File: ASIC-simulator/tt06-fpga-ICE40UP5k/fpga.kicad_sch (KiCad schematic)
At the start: 37 parts, among them U1 ICE40UP5K-SG48I, U2 AP2112K-1.2, X1 24MHz

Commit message: LCSC components and minor layout tweaks for production run
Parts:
- C1, C10, C12, C14, C15, C17, C3, C6, C8: LCSC (none) -> C60474
- C11, C7: LCSC (none) -> C29936
- C13, C16, C18, C2, C4, C9: LCSC (none) -> C237615
- C5: LCSC (none) -> C92487
- R10, R3: LCSC (none) -> C60490
- R11: LCSC (none) -> C106231
- R2, R6, R9: LCSC (none) -> C106232
- R5: LCSC (none) -> C106235
- R7, R8: LCSC (none) -> C163455
- TP1, TP2: now left out of the parts list

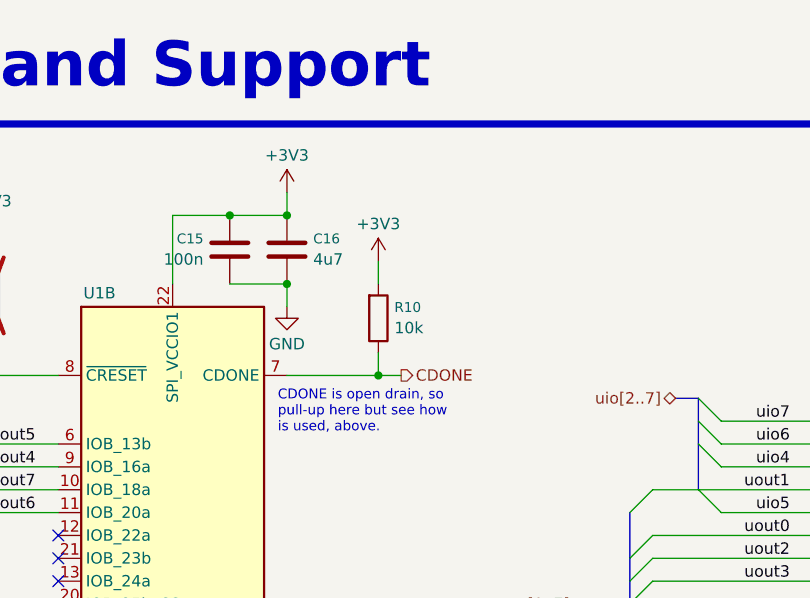
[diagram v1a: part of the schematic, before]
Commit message: v1.1 CDONE LED
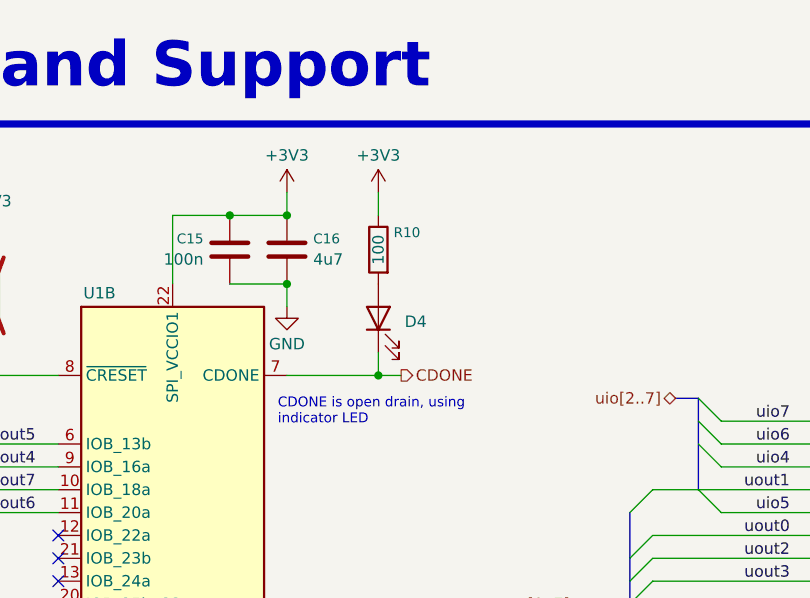
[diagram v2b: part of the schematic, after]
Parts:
- removed R10: 10k, Resistor_SMD:R_0402_1005Metric, symbol psycomponents:PsyResistors_IEC/R_10k_0402_1005-12
- added D4: LED, LED_SMD:LED_0603_1608Metric, symbol Device:LED
- added R10: 100, Resistor_SMD:R_0402_1005Metric, symbol psycomponents:PsyResistors_IEC/R_100_0402_1005-9
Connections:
- net +3V3: now also R10.2
- net CDONE: now also D4.1 (K)
- new net: D4.2 (A), R10.1
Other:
- note added: "CDONE is open drain, using indicator LED"
- note removed: "CDONE is open drain, so pull-up here but see how is used, above."
